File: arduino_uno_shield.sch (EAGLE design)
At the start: 18 parts

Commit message: created board from scratch
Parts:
- added EXT_LED: M023.5MM, SparkFun-Connectors:M023.5MM
- renumbered MIC to A1, POT1 to A2, POT2 to A3, POT3 to A4, POT4 to A5, POT5 to A6, POT6 to A7, POT7 to A8
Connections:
- net N$7 renamed A6
- net GND: now also EXT_LED.1
- net N$12: now also EXT_LED.2

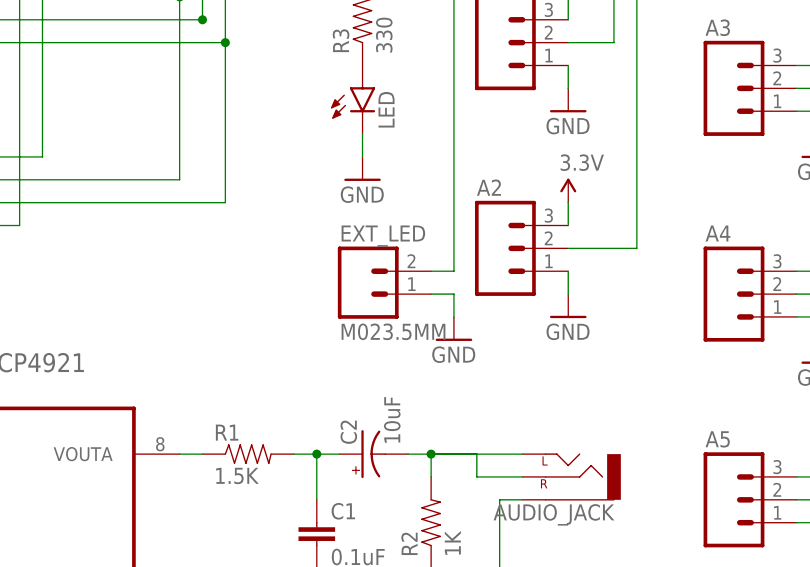
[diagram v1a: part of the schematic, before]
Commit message: fixed polarity issue on LED screw terminal
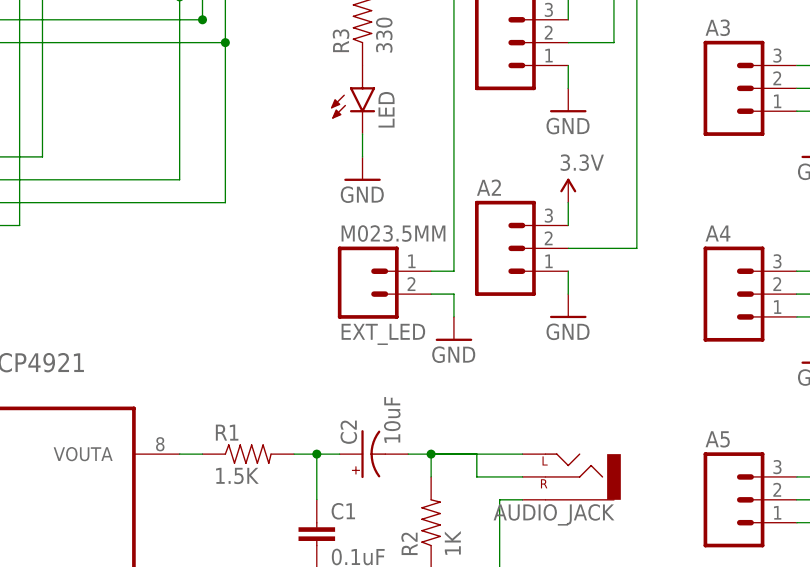
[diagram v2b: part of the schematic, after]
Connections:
- net GND: now also EXT_LED.2; no longer EXT_LED.1
- net N$12: now also EXT_LED.1; no longer EXT_LED.2
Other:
- moved on the sheet: EXT_LED
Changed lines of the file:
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@@
 <instance part="GND12" gate="1" x="-12.7" y="-25.4"/>
 <instance part="GND14" gate="1" x="-53.34" y="22.86"/>
-<instance part="EXT_LED" gate="G$1" x="-63.5" y="27.94"/>
+<instance part="EXT_LED" gate="G$1" x="-63.5" y="30.48" rot="MR180"/>
 </instances>
 <busses>
@@
 </segment>
 <segment>
-<pinref part="EXT_LED" gate="G$1" pin="1"/>
+<pinref part="EXT_LED" gate="G$1" pin="2"/>
 <wire x1="-55.88" y1="27.94" x2="-53.34" y2="27.94" width="0.1524" layer="91"/>
 <pinref part="GND14" gate="1" pin="GND"/>
@@
 <pinref part="R3" gate="G$1" pin="2"/>
 <wire x1="-63.5" y1="66.04" x2="-63.5" y2="63.5" width="0.1524" layer="91"/>
-<pinref part="EXT_LED" gate="G$1" pin="2"/>
+<pinref part="EXT_LED" gate="G$1" pin="1"/>
 <wire x1="-55.88" y1="30.48" x2="-53.34" y2="30.48" width="0.1524" layer="91"/>
 <wire x1="-53.34" y1="30.48" x2="-53.34" y2="66.04" width="0.1524" layer="91"/>

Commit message: save latest
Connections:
- net A6 renamed SPI_MOSI
- net N$13 renamed CS_ADC
- net N$4 renamed SPI_CLK
- net N$5 renamed CS_DAC
- net N$6 renamed SPI_MISO
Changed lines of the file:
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@@
 </segment>
 </net>
-<net name="N$4" class="0">
+<net name="SPI_CLK" class="0">
 <segment>
 <pinref part="U$1" gate="G$1" pin="D13"/>
@@
 </segment>
 </net>
-<net name="N$6" class="0">
+<net name="SPI_MISO" class="0">
 <segment>
 <pinref part="U$1" gate="G$1" pin="D12"/>
@@
 </segment>
 </net>
-<net name="A6" class="0">
+<net name="SPI_MOSI" class="0">
 <segment>
-<pinref part="U$1" gate="G$1" pin="*D11"/>
-<wire x1="-116.84" y1="60.96" x2="-83.82" y2="60.96" width="0.1524" layer="91"/>
-<junction x="-83.82" y="60.96"/>
-<pinref part="MCP3208" gate="A" pin="DIN"/>
-<wire x1="15.24" y1="73.66" x2="-83.82" y2="73.66" width="0.1524" layer="91"/>
-<wire x1="-83.82" y1="73.66" x2="-83.82" y2="60.96" width="0.1524" layer="91"/>
-<wire x1="-83.82" y1="60.96" x2="-83.82" y2="40.64" width="0.1524" layer="91"/>
 <wire x1="-83.82" y1="40.64" x2="-134.62" y2="40.64" width="0.1524" layer="91"/>
 <wire x1="-134.62" y1="40.64" x2="-134.62" y2="-2.54" width="0.1524" layer="91"/>
 <pinref part="MCP4921" gate="A" pin="SDI"/>
 <wire x1="-134.62" y1="-2.54" x2="-119.38" y2="-2.54" width="0.1524" layer="91"/>
+<pinref part="MCP3208" gate="A" pin="DIN"/>
+<wire x1="15.24" y1="73.66" x2="-83.82" y2="73.66" width="0.1524" layer="91"/>
+<pinref part="U$1" gate="G$1" pin="*D11"/>
+<wire x1="-116.84" y1="60.96" x2="-83.82" y2="60.96" width="0.1524" layer="91"/>
+<wire x1="-83.82" y1="60.96" x2="-83.82" y2="73.66" width="0.1524" layer="91"/>
+<wire x1="-83.82" y1="60.96" x2="-83.82" y2="40.64" width="0.1524" layer="91"/>
+<junction x="-83.82" y="60.96"/>
 </segment>
 </net>
@@
 </segment>
 </net>
-<net name="N$13" class="0">
+<net name="CS_ADC" class="0">
 <segment>
 <pinref part="MCP3208" gate="A" pin="~CS/SHDN"/>
@@
 </segment>
 </net>
-<net name="N$5" class="0">
+<net name="CS_DAC" class="0">
 <segment>
 <pinref part="MCP4921" gate="A" pin="~CS"/>

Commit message: save
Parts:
- added FRAME3: FRAME-LETTER, SparkFun-Aesthetics:FRAME-LETTER
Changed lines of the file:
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@@
 <part name="GND14" library="SparkFun-Aesthetics" deviceset="GND" device=""/>
 <part name="EXT_LED" library="SparkFun-Connectors" deviceset="M02" device="3.5MM"/>
+<part name="FRAME3" library="SparkFun-Aesthetics" deviceset="FRAME-LETTER" device=""/>
 </parts>
 <sheets>
@@
 <instance part="GND14" gate="1" x="-53.34" y="22.86"/>
 <instance part="EXT_LED" gate="G$1" x="-63.5" y="30.48" rot="MR180"/>
+<instance part="FRAME3" gate="G$1" x="-170.18" y="-78.74"/>
+<instance part="FRAME3" gate="G$2" x="-22.86" y="-78.74"/>
 </instances>
 <busses>
